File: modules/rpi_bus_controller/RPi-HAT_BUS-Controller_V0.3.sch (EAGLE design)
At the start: 64 parts, among them IC1 MC34063AD, IC2 ADUM1201ARZ, IC3 P89LPC922FDH,512FDH, IC4 24LC-I/OT, IC5 LPC1115, Q1 ASF1, T1 BC856, T2 BCP52, T3 BC847

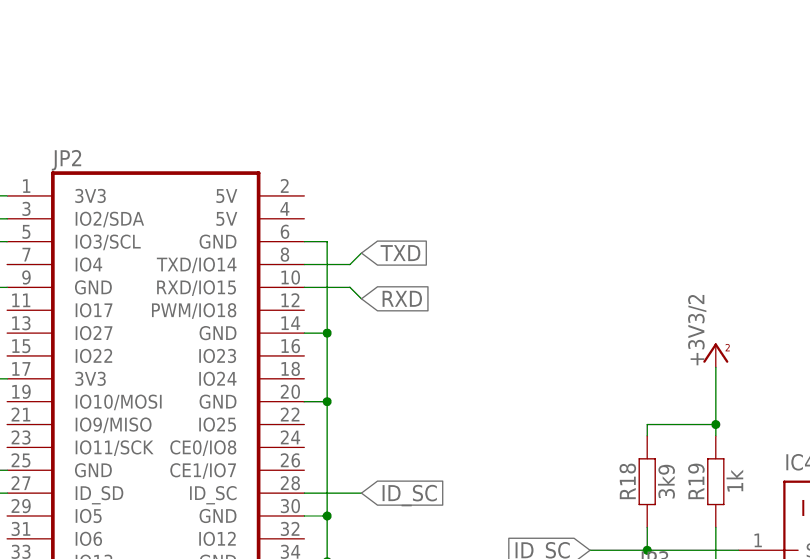
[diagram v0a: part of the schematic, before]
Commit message: TXD RXD getauscht
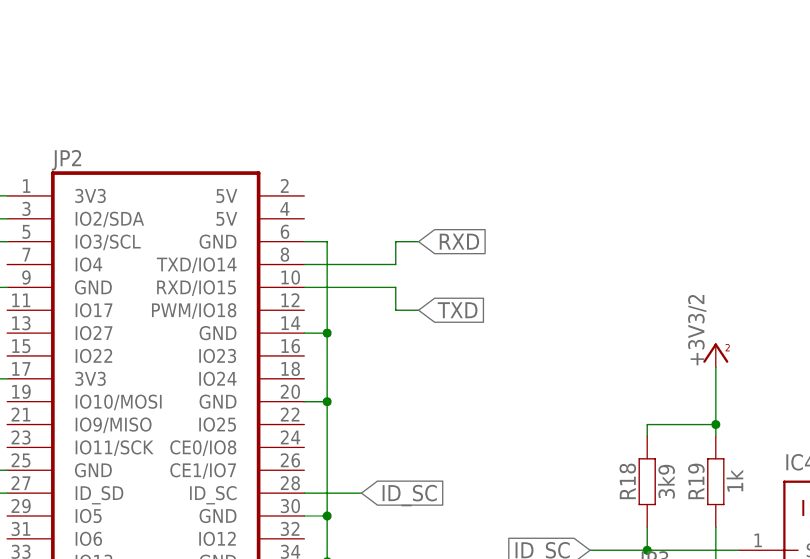
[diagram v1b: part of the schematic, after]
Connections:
- net RXD: now also JP2.TXD/IO14; no longer JP2.RXD/IO15
- net TXD: now also JP2.RXD/IO15; no longer JP2.TXD/IO14
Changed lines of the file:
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@@
 <net name="TXD" class="0">
-<segment>
-<pinref part="JP2" gate="G$1" pin="TXD/IO14"/>
-<wire x1="165.1" y1="144.78" x2="170.18" y2="144.78" width="0.1524" layer="91"/>
-<wire x1="170.18" y1="144.78" x2="171.45" y2="146.05" width="0.1524" layer="91"/>
-<label x="171.45" y="146.05" size="1.778" layer="95" xref="yes"/>
-</segment>
 <segment>
 <pinref part="IC3" gate="A" pin="P1.0/TXD"/>
@@
 <wire x1="266.7" y1="63.5" x2="265.43" y2="64.77" width="0.1524" layer="91"/>
 <label x="265.43" y="64.77" size="1.778" layer="95" rot="R180" xref="yes"/>
+<label x="177.8" y="139.7" size="1.778" layer="95" xref="yes"/>
 </segment>
 <segment>
@@
 <wire x1="525.78" y1="92.71" x2="525.78" y2="88.9" width="0.1524" layer="91"/>
 </segment>
+<segment>
+<pinref part="JP2" gate="G$1" pin="RXD/IO15"/>
+<wire x1="165.1" y1="142.24" x2="175.26" y2="142.24" width="0.1524" layer="91"/>
+<wire x1="175.26" y1="142.24" x2="175.26" y2="139.7" width="0.1524" layer="91"/>
+<wire x1="175.26" y1="139.7" x2="177.8" y2="139.7" width="0.1524" layer="91"/>
+</segment>
 </net>
 <net name="RXD" class="0">
-<segment>
-<pinref part="JP2" gate="G$1" pin="RXD/IO15"/>
-<wire x1="165.1" y1="142.24" x2="170.18" y2="142.24" width="0.1524" layer="91"/>
-<wire x1="170.18" y1="142.24" x2="171.45" y2="140.97" width="0.1524" layer="91"/>
-<label x="171.45" y="140.97" size="1.778" layer="95" xref="yes"/>
-</segment>
 <segment>
 <pinref part="IC3" gate="A" pin="P1.1/RXD"/>
 <wire x1="267.97" y1="60.96" x2="265.43" y2="60.96" width="0.1524" layer="91"/>
 <label x="265.43" y="60.96" size="1.778" layer="95" rot="R180" xref="yes"/>
+<label x="177.8" y="147.32" size="1.778" layer="95" xref="yes"/>
 </segment>
 <segment>
@@
 <wire x1="533.4" y1="86.36" x2="525.78" y2="86.36" width="0.1524" layer="91"/>
 </segment>
+<segment>
+<pinref part="JP2" gate="G$1" pin="TXD/IO14"/>
+<wire x1="165.1" y1="144.78" x2="175.26" y2="144.78" width="0.1524" layer="91"/>
+<wire x1="175.26" y1="144.78" x2="175.26" y2="147.32" width="0.1524" layer="91"/>
+<wire x1="175.26" y1="147.32" x2="177.8" y2="147.32" width="0.1524" layer="91"/>
+</segment>
 </net>

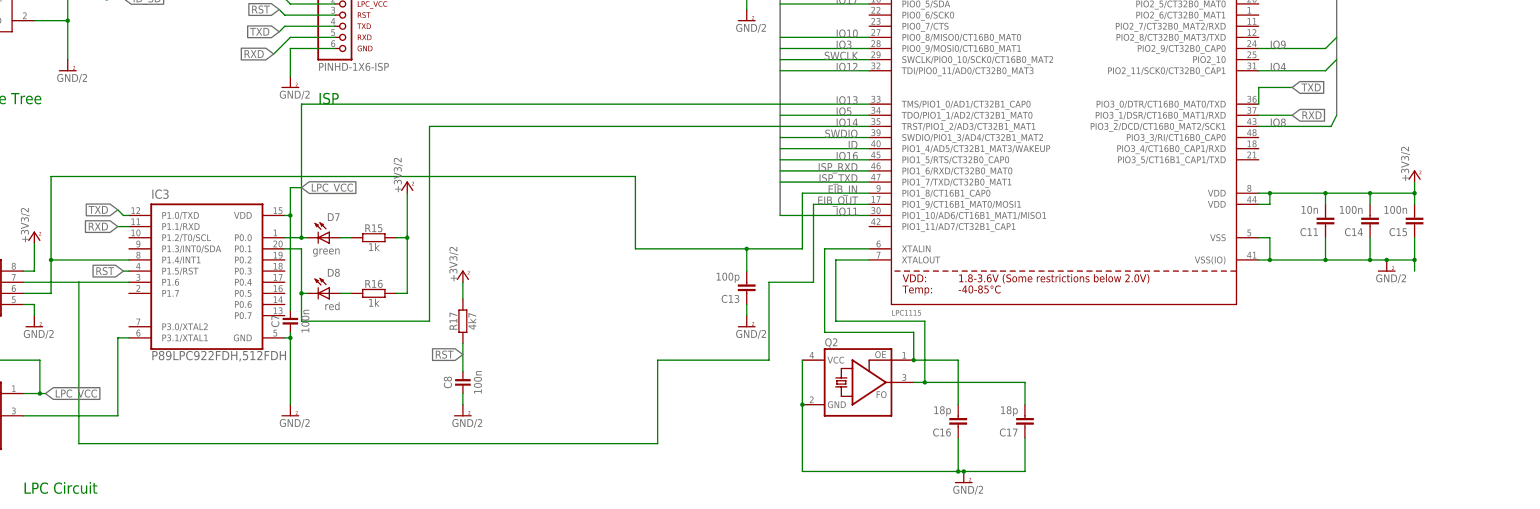
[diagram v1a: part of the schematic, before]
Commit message: Schutzwiderstände in TXD_ARM und EIB-OUT_ARM eingefügt
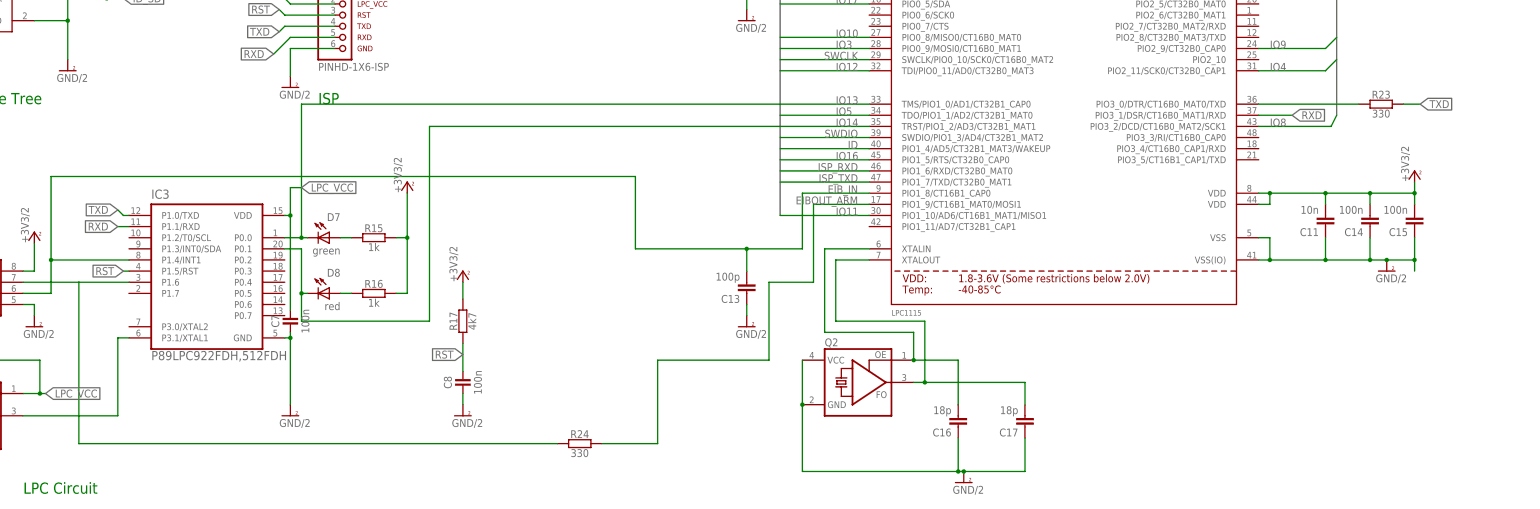
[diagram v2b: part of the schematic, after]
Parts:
- added R23, R24: 330, RCL_for_Selfbus-Projects:RESISTORR1206
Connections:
- new net EIBOUT_ARM: IC5.PIO1_9/CT16B1_MAT0/MOSI1, R24.2
- new net TXD_ARM: IC5.PIO3_0/DTR/CT16B0_MAT0/TXD, R23.1
- net EIB_OUT: now also R24.1; no longer IC5.PIO1_9/CT16B1_MAT0/MOSI1
- net TXD: now also R23.2; no longer IC5.PIO3_0/DTR/CT16B0_MAT0/TXD
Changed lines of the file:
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@@
 <part name="P+5" library="Supply_for_Selfbus-Projects" deviceset="+3V3/2" device=""/>
 <part name="P+7" library="Supply_for_Selfbus-Projects" deviceset="+3V3/2" device=""/>
+<part name="R23" library="RCL_for_Selfbus-Projects" deviceset="RESISTOR" device="R1206" value="330"/>
+<part name="R24" library="RCL_for_Selfbus-Projects" deviceset="RESISTOR" device="R1206" value="330"/>
 </parts>
 <sheets>
@@
 <instance part="P+5" gate="1" x="551.18" y="144.78"/>
 <instance part="P+7" gate="1" x="561.34" y="71.12"/>
+<instance part="R23" gate="G$1" x="553.72" y="88.9"/>
+<instance part="R24" gate="G$1" x="370.84" y="11.43"/>
 </instances>
 <busses>
@@
 <wire x1="303.53" y1="106.68" x2="302.26" y2="105.41" width="0.1524" layer="91"/>
 <label x="302.26" y="105.41" size="1.778" layer="95" rot="R180" xref="yes"/>
-<label x="533.4" y="92.71" size="1.778" layer="95" xref="yes"/>
-</segment>
-<segment>
-<pinref part="IC5" gate="G$1" pin="PIO3_0/DTR/CT16B0_MAT0/TXD"/>
-<wire x1="533.4" y1="92.71" x2="525.78" y2="92.71" width="0.1524" layer="91"/>
-<wire x1="525.78" y1="92.71" x2="525.78" y2="88.9" width="0.1524" layer="91"/>
+<label x="562.61" y="88.9" size="1.778" layer="95" xref="yes"/>
+</segment>
+<segment>
+<wire x1="562.61" y1="88.9" x2="558.8" y2="88.9" width="0.1524" layer="91"/>
+<pinref part="R23" gate="G$1" pin="2"/>
 </segment>
 <segment>
@@
 <net name="EIB_OUT" class="0">
 <segment>
-<wire x1="414.02" y1="30.48" x2="414.02" y2="48.26" width="0.1524" layer="91"/>
-<wire x1="414.02" y1="48.26" x2="424.18" y2="48.26" width="0.1524" layer="91"/>
-<wire x1="424.18" y1="48.26" x2="424.18" y2="66.04" width="0.1524" layer="91"/>
-<wire x1="414.02" y1="30.48" x2="388.62" y2="30.48" width="0.1524" layer="91"/>
-<wire x1="424.18" y1="66.04" x2="436.88" y2="66.04" width="0.1524" layer="91"/>
-<label x="434.34" y="66.04" size="1.778" layer="95" rot="MR0"/>
-<pinref part="IC5" gate="G$1" pin="PIO1_9/CT16B1_MAT0/MOSI1"/>
 <pinref part="IC3" gate="A" pin="P1.6"/>
 <pinref part="IC2" gate="A" pin="VIA"/>
@@
 <wire x1="256.54" y1="48.26" x2="243.84" y2="48.26" width="0.1524" layer="91"/>
 <wire x1="256.54" y1="48.26" x2="256.54" y2="11.43" width="0.1524" layer="91"/>
-<wire x1="256.54" y1="11.43" x2="388.62" y2="11.43" width="0.1524" layer="91"/>
-<wire x1="388.62" y1="11.43" x2="388.62" y2="30.48" width="0.1524" layer="91"/>
+<wire x1="256.54" y1="11.43" x2="365.76" y2="11.43" width="0.1524" layer="91"/>
+<pinref part="R24" gate="G$1" pin="1"/>
 </segment>
 </net>
@@
 </segment>
 </net>
+<net name="TXD_ARM" class="0">
+<segment>
+<pinref part="R23" gate="G$1" pin="1"/>
+<pinref part="IC5" gate="G$1" pin="PIO3_0/DTR/CT16B0_MAT0/TXD"/>
+<wire x1="548.64" y1="88.9" x2="525.78" y2="88.9" width="0.1524" layer="91"/>
+</segment>
+</net>
+<net name="EIBOUT_ARM" class="0">
+<segment>
+<pinref part="IC5" gate="G$1" pin="PIO1_9/CT16B1_MAT0/MOSI1"/>
+<wire x1="424.18" y1="66.04" x2="436.88" y2="66.04" width="0.1524" layer="91"/>
+<wire x1="424.18" y1="48.26" x2="424.18" y2="66.04" width="0.1524" layer="91"/>
+<wire x1="414.02" y1="48.26" x2="424.18" y2="48.26" width="0.1524" layer="91"/>
+<wire x1="414.02" y1="30.48" x2="414.02" y2="48.26" width="0.1524" layer="91"/>
+<wire x1="414.02" y1="30.48" x2="388.62" y2="30.48" width="0.1524" layer="91"/>
+<wire x1="388.62" y1="11.43" x2="388.62" y2="30.48" width="0.1524" layer="91"/>
+<wire x1="375.92" y1="11.43" x2="388.62" y2="11.43" width="0.1524" layer="91"/>
+<pinref part="R24" gate="G$1" pin="2"/>
+<label x="434.34" y="66.04" size="1.778" layer="95" rot="MR0"/>
+</segment>
+</net>
